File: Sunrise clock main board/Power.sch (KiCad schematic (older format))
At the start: 29 parts, among them J1 Barrel_Jack_Switch, U1 NCP1117LPST33T3G, U2 MAX809S, U3 LM258DR, U7 74AHC125D

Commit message: Tweaks
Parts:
- F2: footprint Fuse:Fuse_1812_4532Metric_Pad1.30x3.40mm_HandSolder -> Fuse-fixed:Fuse_1812_4532Metric_Pad1.30x3.40mm_HandSolder
- U3: value LM258DR -> LM358DR; footprint Package_SO-extra:Dual_SO-8_3.9x4.9mm_P1.27mm+DIP8 -> Package_SO:SOIC-8_3.9x4.9mm_P1.27mm
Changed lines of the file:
@@
 AR Path="/5FEEBD3E/5FF1190D" Ref="U3"  Part="1"
 F 0 "U3" H 4050 6917 50  0000 C CNN
-F 1 "LM258DR" H 4050 6826 50  0000 C CNN
-F 2 "Package_SO-extra:Dual_SO-8_3.9x4.9mm_P1.27mm+DIP8" H 4050 6550 50  0001 C CNN
+F 1 "LM358DR" H 4050 6826 50  0000 C CNN
+F 2 "Package_SO:SOIC-8_3.9x4.9mm_P1.27mm" H 4050 6550 50  0001 C CNN
 F 3 "~" H 4050 6550 50  0001 C CNN
 	1    4050 6550
@@
 AR Path="/5FEEBD3E/5FF1196A" Ref="U3"  Part="3"
 F 0 "U3" H 1508 6796 50  0000 L CNN
-F 1 "LM258DR" H 1508 6705 50  0000 L CNN
-F 2 "Package_SO-extra:Dual_SO-8_3.9x4.9mm_P1.27mm+DIP8" H 1550 6750 50  0001 C CNN
+F 1 "LM358DR" H 1508 6705 50  0000 L CNN
+F 2 "Package_SO:SOIC-8_3.9x4.9mm_P1.27mm" H 1550 6750 50  0001 C CNN
 F 3 "~" H 1550 6750 50  0001 C CNN
 	3    1550 6750
@@
 AR Path="/5FEEBD3E/5FF11970" Ref="U3"  Part="2"
 F 0 "U3" H 9150 4467 50  0000 C CNN
-F 1 "LM258DR" H 9150 4376 50  0000 C CNN
-F 2 "Package_SO-extra:Dual_SO-8_3.9x4.9mm_P1.27mm+DIP8" H 9150 4100 50  0001 C CNN
+F 1 "LM358DR" H 9150 4376 50  0000 C CNN
+F 2 "Package_SO:SOIC-8_3.9x4.9mm_P1.27mm" H 9150 4100 50  0001 C CNN
 F 3 "~" H 9150 4100 50  0001 C CNN
 	2    9150 4100
@@
 F 0 "F2" V 3075 2000 50  0000 C CNN
 F 1 "Polyfuse 1.5A >=6V" V 3166 2000 50  0000 C CNN
-F 2 "Fuse:Fuse_1812_4532Metric_Pad1.30x3.40mm_HandSolder" H 3350 1800 50  0001 L CNN
+F 2 "Fuse-fixed:Fuse_1812_4532Metric_Pad1.30x3.40mm_HandSolder" H 3350 1800 50  0001 L CNN
 F 3 "~" H 3300 2000 50  0001 C CNN
 	1    3300 2000

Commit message: Now in stereo if you want.
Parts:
- added R67, R68: 100k, Resistor_SMD:R_0805_2012Metric_Pad1.20x1.40mm_HandSolder, symbol Device:R
- added TP20: TestPoint, TestPoint:TestPoint_THTPad_1.5x1.5mm_Drill0.7mm, symbol Connector:TestPoint
- renumbered C40 to C33, R1 to R15, R29 to R20, R70 to R80
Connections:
- net GND: now also R67.2, R68.2, TP20.1
- net ~RESET_5V: now also R68.1
- net at D2.3 (K), U2.2 (~RESET), U7.12: now also R67.1
- net NEOPIXEL_GND renamed EXTERNAL_GND
- net NEOPIXEL_POWER renamed EXTERNAL_CURRENT
- net RC_NEO_GND: no longer names the net of C5.1, R35.2, TP2.1, U3.5 (+)
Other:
- note added: "2.02V@4A"
- note added: "20mV@4A"
- note added: "External IO current measurement"
- note added: "Voltage monitor"
- note removed: "ESP32 voltage monitor"
- note removed: "Neopixel power measurement"
- moved on the sheet: R12, R15, R30, R40, R80, TP8, U3A

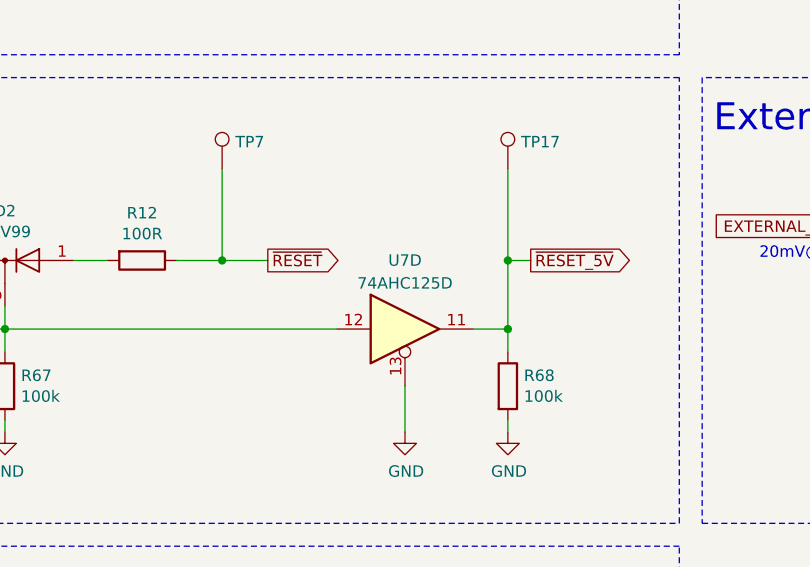
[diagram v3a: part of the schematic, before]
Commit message: Started with checklist.
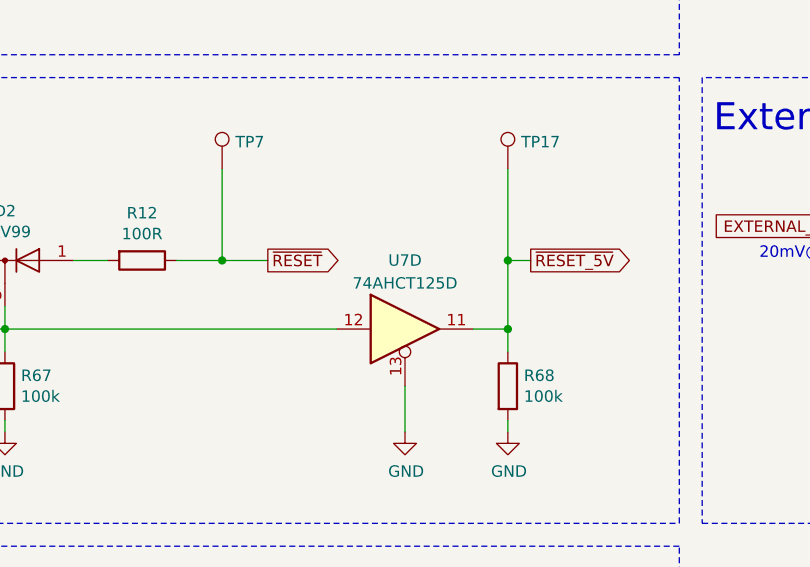
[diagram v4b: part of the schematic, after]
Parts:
- U7: value 74AHC125D -> 74AHCT125D
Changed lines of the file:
@@
 AR Path="/5FEEBD3E/5FECB747" Ref="U7"  Part="4"
 F 0 "U7" H 5650 4750 50  0000 C CNN
-F 1 "74AHC125D" H 5650 4650 50  0000 C CNN
+F 1 "74AHCT125D" H 5650 4650 50  0000 C CNN
 F 2 "Package_SO-fixed:SO-14_3.9x8.65mm_P1.27mm" H 5650 4450 50  0001 C CNN
 F 3 "" H 5650 4450 50  0001 C CNN

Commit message: More testing.
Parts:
- removed R13: 100R, Resistor_SMD:R_0805_2012Metric_Pad1.20x1.40mm_HandSolder, symbol Device:R
- removed R20: 1k, Resistor_SMD:R_0805_2012Metric_Pad1.20x1.40mm_HandSolder, symbol Device:R
- removed R35: 4k7, Resistor_SMD:R_0805_2012Metric_Pad1.20x1.40mm_HandSolder, symbol Device:R
- removed R60: 100k, Resistor_SMD:R_0805_2012Metric_Pad1.20x1.40mm_HandSolder, symbol Device:R
- removed TP2, TP5: TestPoint, TestPoint:TestPoint_THTPad_1.5x1.5mm_Drill0.7mm, symbol Connector:TestPoint
- added C18: 100nF, Capacitor_SMD:C_0805_2012Metric_Pad1.18x1.45mm_HandSolder, symbol Device:C
- added NT1, NT2: Net-Tie_2, NetTie-fixed:NetTie-2_SMD_Pad0.5mm, symbol Device:Net-Tie_2
- added R1: 0R05, Resistor_SMD:R_2512_6332Metric_Pad1.52x3.35mm_HandSolder, symbol Device:R
- added R16, R17: 10R, Resistor_SMD:R_0805_2012Metric_Pad1.20x1.40mm_HandSolder, symbol Device:R
- added U11: INA219AIDCNR, Package_TO_SOT_SMD:SOT-23-8, symbol Analog_ADC:INA219AxDCN
- C5: value 10uF -> 1uF
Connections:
- net +3V3: now also C18.1, U11.4 (VS)
- net +5V: no longer F2.1
- net +5VL: now also NT1.1, R1.1; no longer J1.1
- net GND: now also C10.2, R40.2, R80.2, U3.4 (V-), U3.5 (+), C18.2, U11.3 (GND), U11.7 (A0), U11.8 (A1); no longer D1.2 (A)
- net at U3.6 (-): now also U3.7
- net at C5.1: now also R16.1, U11.1 (IN+); no longer U3.5 (+)
- removed net GND2: C10.2, C5.2, R40.2, R80.2, U3.4 (V-)
- new net: J1.1, NT2.1, R1.2
- new net: D1.2 (A), F2.1
- new net: C5.2, R17.1, U11.2 (IN-)
- new net SCL_3V: U11.5 (SCL)
- new net SDA_3V: U11.6 (SDA)
- new net VIN+: NT2.2, R16.2
- new net VIN-: NT1.2, R17.2
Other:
- note added: "I2C: 0x40"
- note added: "Use 5V 3A high quality adapter, \ncenter pin positive.\nSuggestion: \nMean Well GST25E05"
- note added: "Voltage and current measurement"
- note removed: "2.02V@4A"
- note removed: "20mV@4A"
- note removed: "External IO current measurement"
- note removed: "Use 5V 3A high quality adapter, \ncenter pin positive."
- note removed: "gain: 101"
- moved on the sheet: D1, F2, R15, R30, R40, R80, TP8, U3A, U3B

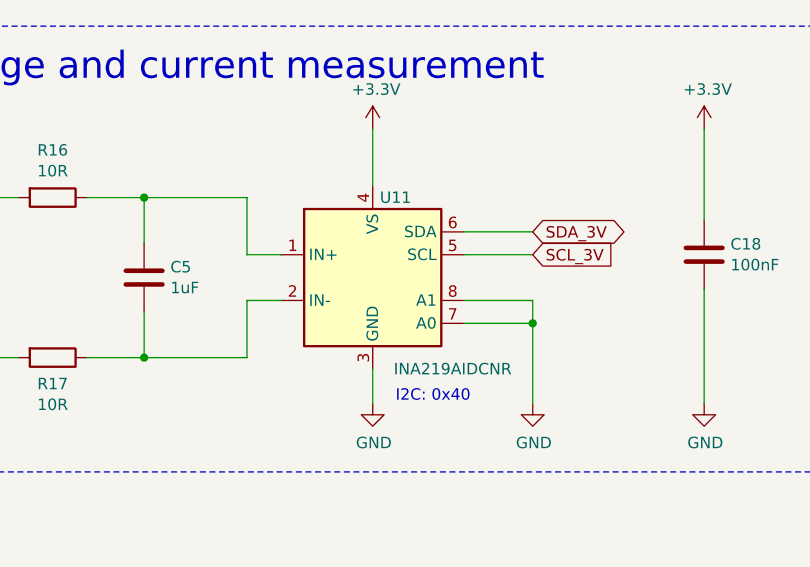
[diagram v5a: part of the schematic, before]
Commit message: Changed INA219AxDCN to INA219AxD
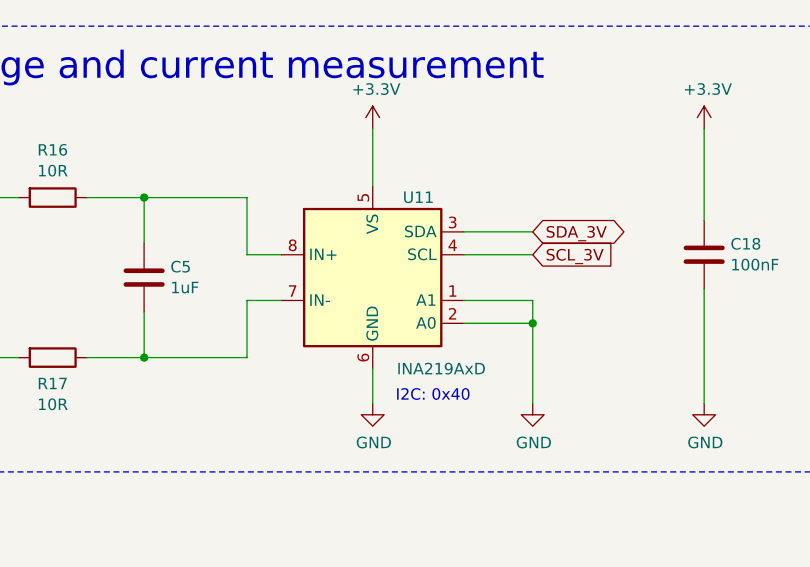
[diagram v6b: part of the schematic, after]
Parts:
- removed U11: INA219AIDCNR, Package_TO_SOT_SMD:SOT-23-8, symbol Analog_ADC:INA219AxDCN
- added U11: INA219AxD, Package_SO:SOIC-8_3.9x4.9mm_P1.27mm, symbol Analog_ADC:INA219AxD
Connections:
- net +3V3: now also U11.5 (VS)
- net GND: now also U11.1 (A1), U11.2 (A0), U11.6 (GND)
- net SCL_3V: now also U11.4 (SCL)
- net SDA_3V: now also U11.3 (SDA)
- net at C5.1, R16.1: now also U11.8 (IN+)
- net at C5.2, R17.1: now also U11.7 (IN-)
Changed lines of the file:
@@
 Sheet 2 6
 Title "Sunrise clock main board"
-Date "2021-05-04"
+Date "2021-08-06"
 Rev "V1.1"
 Comp "https://github.com/atoomnetmarc/Sunrise-clock-hardware"
@@
 VIN+
 $Comp
-L Analog_ADC:INA219AxDCN U11
-U 1 1 60972090
-P 9050 4450
-F 0 "U11" H 9150 4800 50  0000 C CNN
-F 1 "INA219AIDCNR" H 9400 4050 50  0000 C CNN
-F 2 "Package_TO_SOT_SMD:SOT-23-8" H 9700 4100 50  0001 C CNN
-F 3 "http://www.ti.com/lit/ds/symlink/ina219.pdf" H 9400 4350 50  0001 C CNN
-	1    9050 4450
-	1    0    0    -1
-$EndComp
-$Comp
 L power:+3.3V #PWR?
 U 1 1 6097322D
@@
 	8500 4350 8650 4350
 Connection ~ 8050 4100
+$Comp
+L Analog_ADC:INA219AxD U11
+U 1 1 610D83DD
+P 9050 4450
+F 0 "U11" H 9250 4800 50  0000 C CNN
+F 1 "INA219AxD" H 9350 4050 50  0000 C CNN
+F 2 "Package_SO:SOIC-8_3.9x4.9mm_P1.27mm" H 9850 4100 50  0001 C CNN
+F 3 "http://www.ti.com/lit/ds/symlink/ina219.pdf" H 9400 4350 50  0001 C CNN
+	1    9050 4450
+	1    0    0    -1
+$EndComp
 $EndSCHEMATC
